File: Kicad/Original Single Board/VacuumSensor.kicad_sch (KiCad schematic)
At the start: 38 parts, among them IC1 LM2597MX-ADJ_NOPB, IC2 24PCDFA6D, IC3 INA849DR, IC4 TL071CP, IC5 SP3220EBEY-L_TR, J1 Conn_01x02, J2 Conn_01x02, J3 Screw_Terminal_01x05, U1 TL431LP, U2 TL431LP

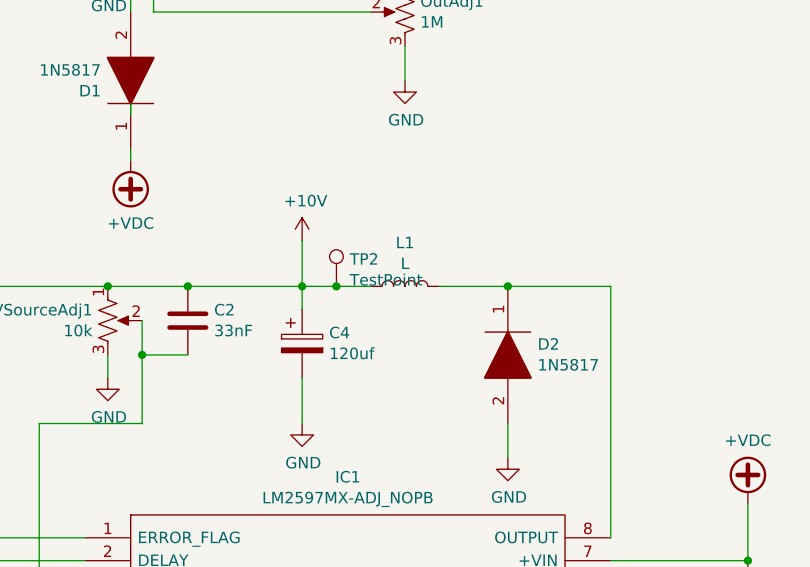
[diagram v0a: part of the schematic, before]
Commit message: updating all the kicad files to 7.0
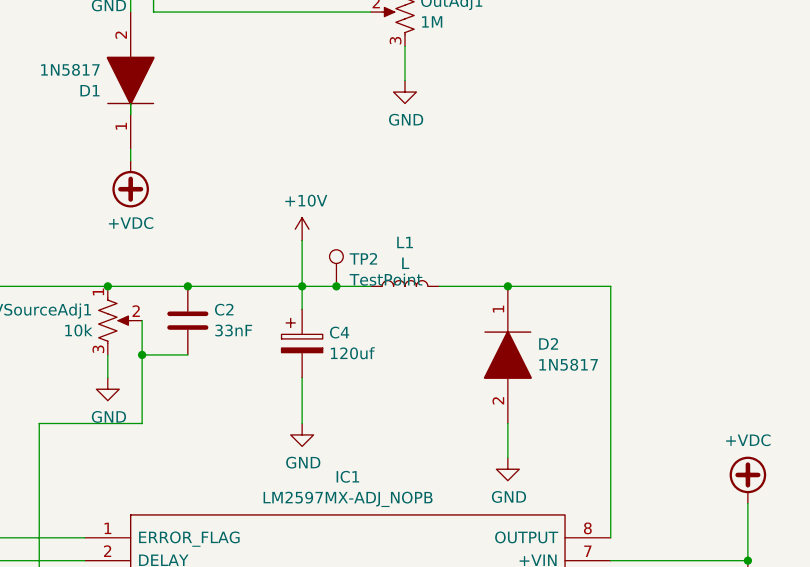
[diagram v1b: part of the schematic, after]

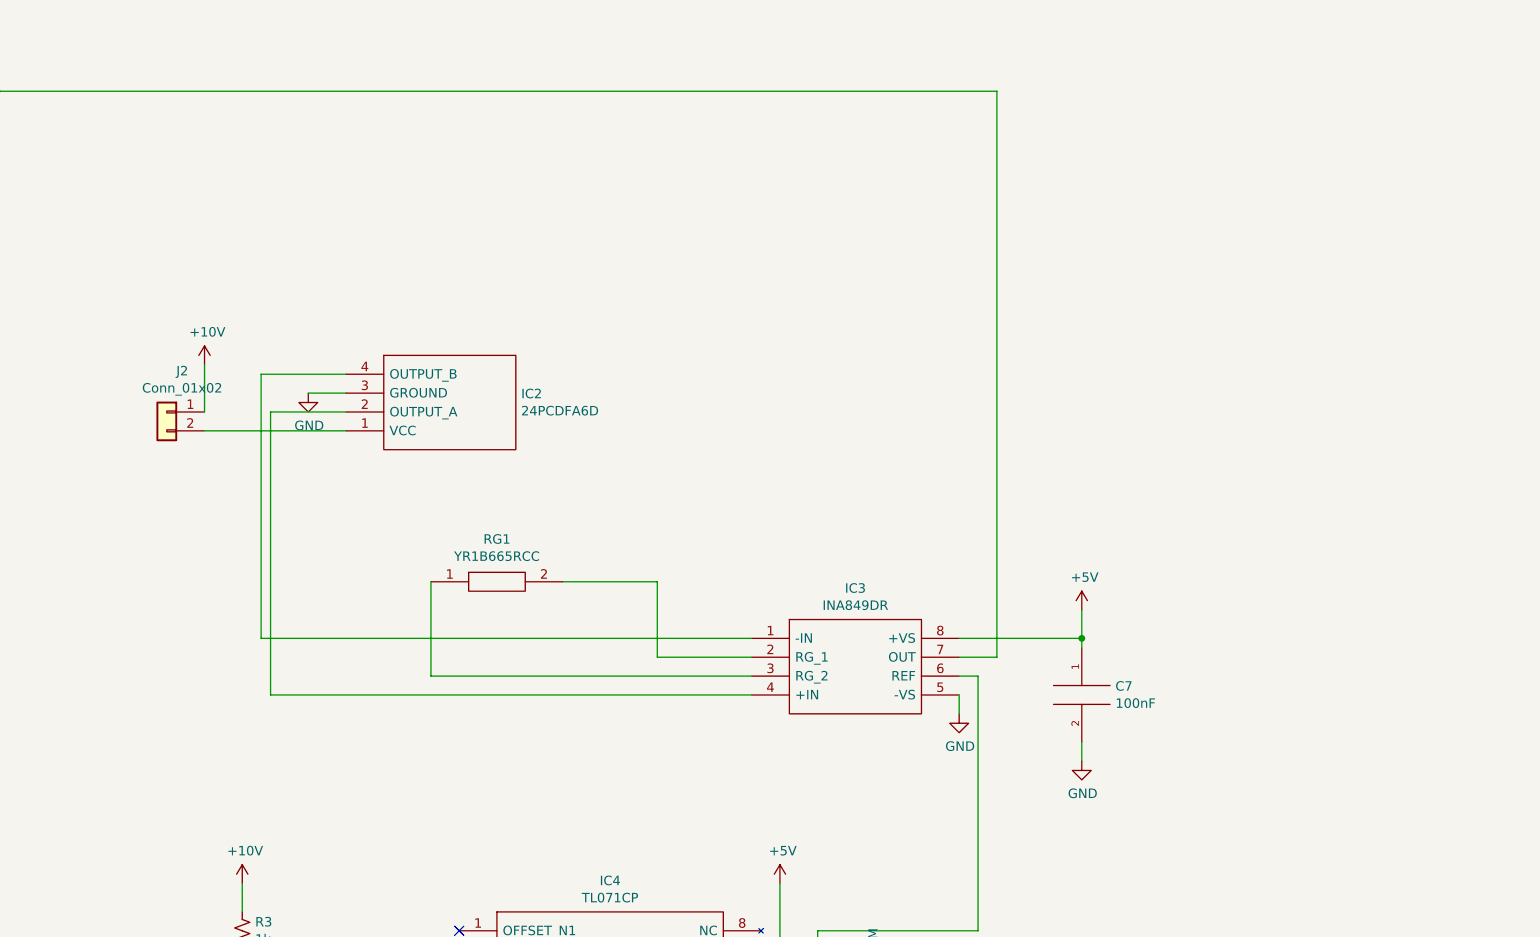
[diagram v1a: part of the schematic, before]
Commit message: * removing the other designs * fixing up the original design
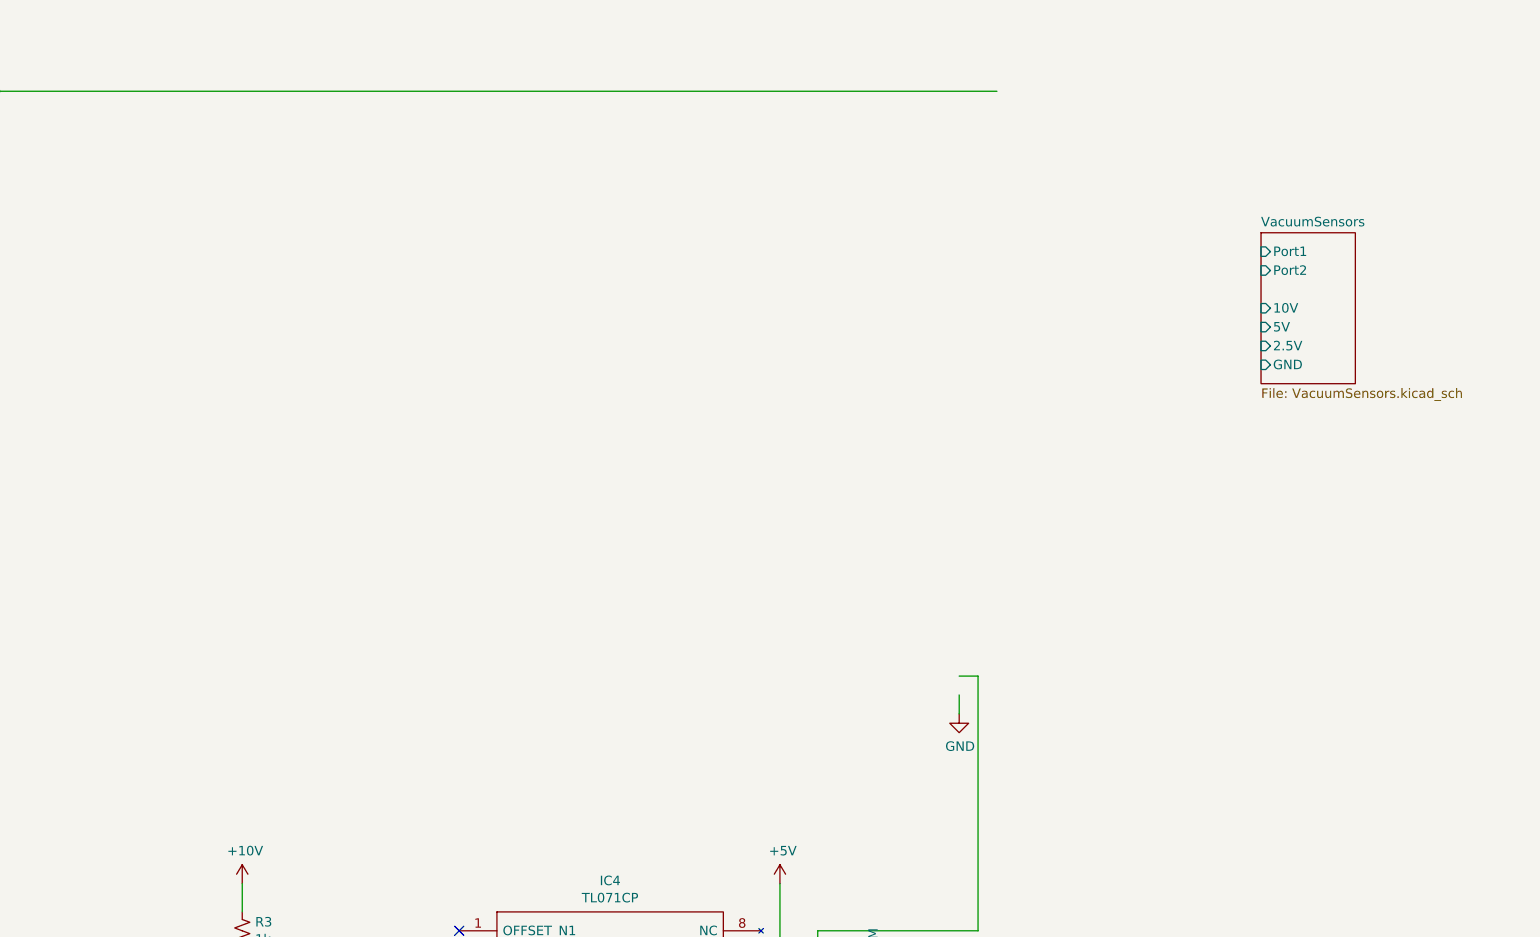
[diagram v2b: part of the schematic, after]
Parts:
- removed C7: 100nF, Capacitor_SMD:C_0805_2012Metric_Pad1.15x1.40mm_HandSolder, symbol pspice:CAP
- removed IC2: 24PCDFA6D, SamacSys_Parts:24PCDFA6D, symbol SamacSys_Parts:24PCDFA6D
- removed IC3: INA849DR, SamacSys_Parts:SOIC127P600X175-8N, symbol SamacSys_Parts:INA849DR
- removed J2: Conn_01x02, Connector_PinHeader_2.54mm:PinHeader_1x02_P2.54mm_Vertical, symbol Connector_Generic:Conn_01x02
- removed RG1: YR1B665RCC, RESAD1550W60L630D230, symbol SamacSys_Parts:YR1B665RCC
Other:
- added sheet VacuumSensors (VacuumSensors.kicad_sch)
